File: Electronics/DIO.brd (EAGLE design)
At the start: 50 x 50 mm, 6 parts

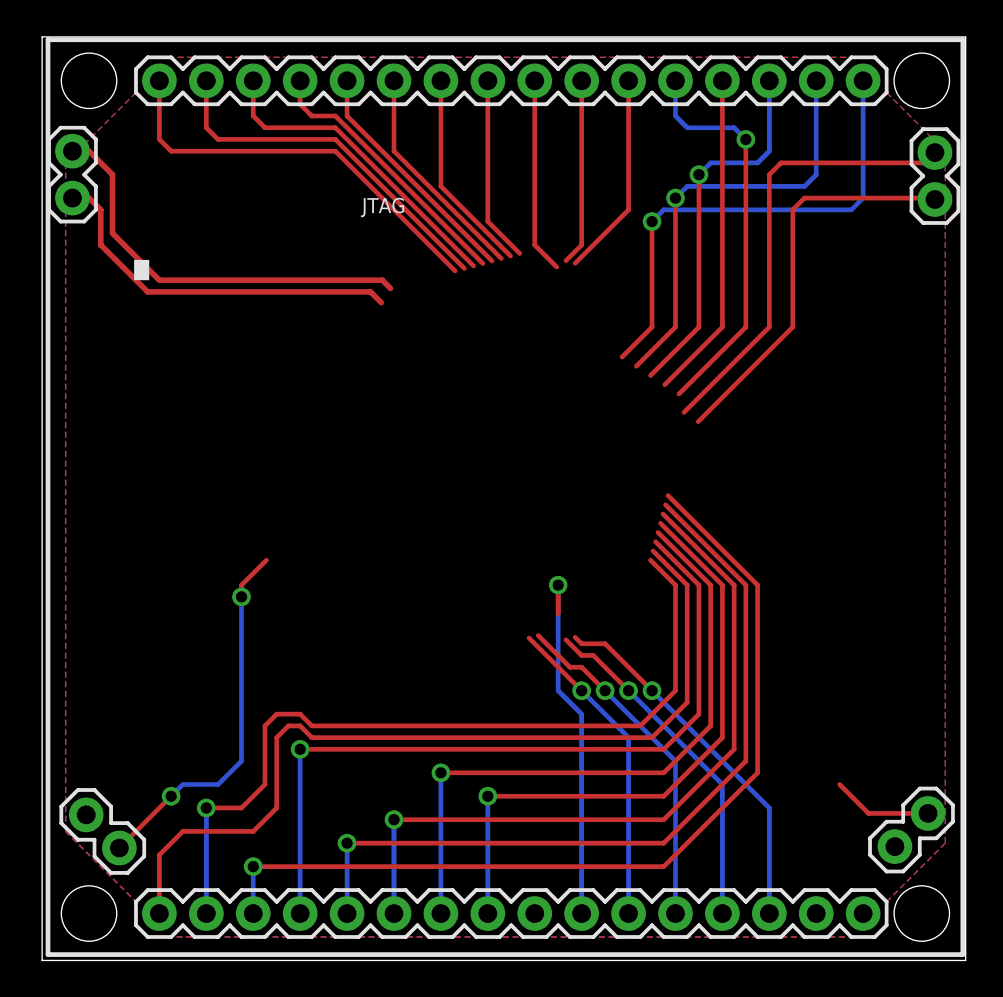
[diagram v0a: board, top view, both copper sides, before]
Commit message: Route DIO Breakout + update Text
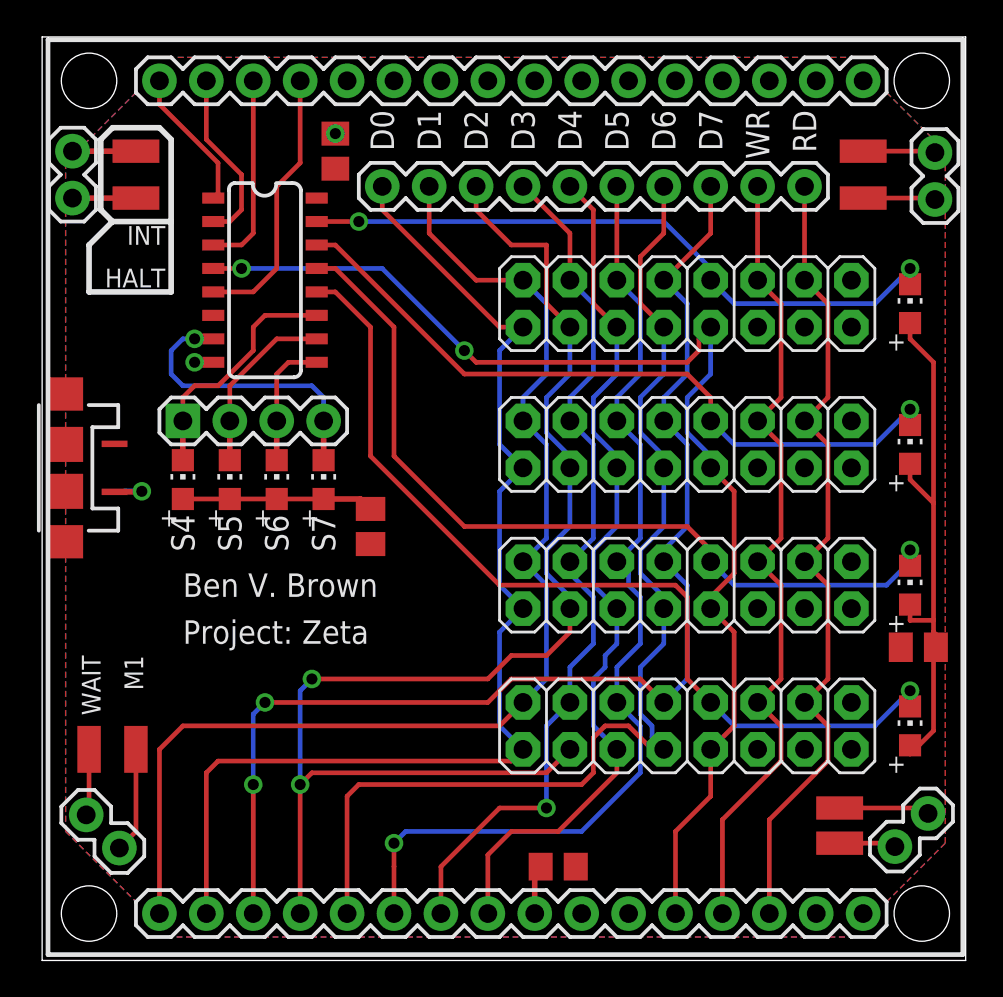
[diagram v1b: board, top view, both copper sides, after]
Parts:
- added C1, C2: (no value), rcl:C0805
- added JP7: (no value), SparkFun-Connectors:1X04
- added JP8: M10", SparkFun:1X10
- added LED1, LED2, LED3, LED4, LED5, LED6, LED7, LED8: (no value), adafruit:CHIP-LED0805
- added PAD1, PAD2, PAD3, PAD4, PAD5, PAD6, PAD7, PAD8: (no value), wirepad:SMD1,27-2,54
- added R1, R2: 10k, rcl:M0805
- added U$1: 74LVC138AD, SparkFun-DigitalIC:SO016
- added U$2, U$3, U$4, U$5: M08X2, SparkFun-Connectors:2X8
- added U$6: USB-MICRO-PWR, RalimTek:USB-MICROB-PWR
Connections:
- new net N$1: LED1.A, LED2.A, LED3.A, LED4.A, R1.2
- new net N$2: LED5.A, LED6.A, LED7.A, LED8.A, R2.2
- new net S0: LED1.C, U$1.15, U$2.10
- new net S1: LED2.C, U$1.14, U$5.10
- new net S2: LED3.C, U$1.13, U$4.10
- new net S3: LED4.C, U$1.12, U$3.10
- new net S4: JP7.1, LED5.C, U$1.11
- new net S5: JP7.2, LED6.C, U$1.10
- new net S6: JP7.3, LED7.C, U$1.9
- new net S7: JP7.4, LED8.C, U$1.7
- net A0: now also U$1.1
- net A1: now also U$1.2
- net A2: now also U$1.3
- net A3: now also U$1.5
- net BUSAK: now also PAD6.1
- net BUSRQ: now also PAD8.1
- net CLK: now also PAD4.1
- net D0: now also JP8.1, U$2.1, U$3.1, U$4.1, U$5.1
- net D1: now also JP8.2, U$2.2, U$3.2, U$4.2, U$5.2
- net D2: now also JP8.3, U$2.3, U$3.3, U$4.3, U$5.3
- net D3: now also JP8.4, U$2.4, U$3.4, U$4.4, U$5.4
- net D4: now also JP8.5, U$2.5, U$3.5, U$4.5, U$5.5
- net D5: now also JP8.6, U$2.6, U$3.6, U$4.6, U$5.6
- net D6: now also JP8.7, U$2.7, U$3.7, U$4.7, U$5.7
- net D7: now also JP8.8, U$2.8, U$3.8, U$4.8, U$5.8
- net GND: now also C1.2, C2.2, U$1.8, U$2.11, U$2.13, U$3.11, U$3.13, U$4.11, U$4.13, U$5.11, U$5.13, U$6.GND
- net HALT: now also PAD7.1
- net INT: now also PAD5.1
- net IORQ: now also U$1.4, U$2.9, U$3.9, U$4.9, U$5.9
- net M1: now also PAD1.1
- net NMI: now also PAD3.1
- net RD: now also JP8.9, U$2.12, U$3.12, U$4.12, U$5.12
- net VCC: now also C1.1, C2.1, R1.1, R2.1, U$1.16, U$2.15, U$2.16, U$3.15, U$3.16, U$4.15, U$4.16, U$5.15, U$5.16, U$6.VBUS
- net WAIT: now also PAD2.1
- net WR: now also JP8.10, U$2.14, U$3.14, U$4.14, U$5.14
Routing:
- net S3: track 0.00 -> 50.2 mm, vias 0 -> 1
- net IORQ: track 18.5 -> 65.9 mm, vias 1 -> 2
- net S2: track 0.00 -> 45.7 mm, vias 0 -> 1
- net S1: track 0.00 -> 39.0 mm, vias 0 -> 1
- net S0: track 0.00 -> 36.0 mm, vias 0 -> 2
- net D2: track 41.6 -> 72.8 mm, vias 1 -> 2
- net N$1: track 0.00 -> 30.3 mm
- net A11: track 26.3 -> 0.00 mm, vias 1 -> 0
- net RD: track 18.7 -> 44.4 mm, vias 1 -> 0
- net WR: track 20.1 -> 44.4 mm, vias 1 -> 0
- net A12: track 23.2 -> 0.00 mm, vias 1 -> 0
- net A15: track 21.5 -> 0.00 mm, vias 1 -> 0
- net BUSAK: track 24.2 -> 3.92 mm
- net A13: track 20.1 -> 0.00 mm, vias 1 -> 0
- net RESET: track 19.9 -> 0.00 mm, vias 1 -> 0
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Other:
- board text added: "Ben V. Brown"
- board text added: "D0 D1 D2 D3 D4 D5 D6 D7 WR RD"
- board text added: "INT HALT"
- board text added: "Project: Zeta"
- board text added: "S4 S5 S6 S7"
- board text added: "WAIT M1"
- board text removed: "."
- board text removed: "JTAG"

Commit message: Gerbers!
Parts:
- moved U$6 8.89 mm to (1.27, 17.8)
- moved PAD1 1.27 mm to (5.08, 10.2)
- moved PAD2 1.27 mm to (2.54, 10.2)
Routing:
- net WAIT: track 3.61 -> 2.34 mm
- net M1: track 5.72 -> 4.45 mm
- net GND: track 6.75 -> 6.18 mm
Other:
- board text added: "1 3 5 7 S R W V 0 2 4 6 I G G V"
